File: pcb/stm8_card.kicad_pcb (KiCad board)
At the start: 2 copper layers, 101.9 x 50.9 mm, 22 parts, among them J1 DEBUG HEADER, SW1 TL59AF100Q, SW2 TL59AF100Q, SW3 TL59AF100Q, SW4 TL3302AF260QG, U1 ER-OLED0.91-7, U2 STM8S103F3

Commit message: pcb small edits
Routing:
- net GND: track 150.1 -> 153.8 mm
- net NRST: track 142.9 -> 141.4 mm
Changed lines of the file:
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@@
     (thickness 1.6)
     (drawings 10)
-    (tracks 348)
+    (tracks 347)
     (zones 0)
     (modules 22)
@@
   (page A4)
   (layers
-    (0 F.Cu signal hide)
+    (0 F.Cu signal)
     (31 B.Cu signal)
     (32 B.Adhes user)
@@
     (47 F.CrtYd user)
     (48 B.Fab user)
-    (49 F.Fab user hide)
+    (49 F.Fab user)
   )
   (setup
@@
   (segment (start 232.25 110.25) (end 231.75 110.25) (width 0.25) (layer F.Cu) (net 1))
   (via (at 232.25 110.25) (size 0.8) (drill 0.4) (layers F.Cu B.Cu) (net 1))
-  (via (at 267 106.25) (size 0.8) (drill 0.4) (layers F.Cu B.Cu) (net 1))
+  (via (at 266.75 106) (size 0.8) (drill 0.4) (layers F.Cu B.Cu) (net 1))
   (segment (start 262.975001 103.274999) (end 262.25 104) (width 0.25) (layer B.Cu) (net 1))
   (segment (start 267 106.25) (end 267 104.676998) (width 0.25) (layer B.Cu) (net 1))
-  (segment (start 268.065 117.815) (end 267.25 117) (width 0.25) (layer F.Cu) (net 1))
-  (via (at 267.25 117) (size 0.8) (drill 0.4) (layers F.Cu B.Cu) (net 1))
-  (segment (start 268.9175 117.815) (end 268.065 117.815) (width 0.25) (layer F.Cu) (net 1))
   (segment (start 267 106.25) (end 267 109.75) (width 0.25) (layer B.Cu) (net 1))
   (segment (start 273.975001 132.594999) (end 269.41 137.16) (width 0.25) (layer B.Cu) (net 1))
@@
   (segment (start 260 132.75) (end 253 132.75) (width 0.25) (layer B.Cu) (net 1))
   (segment (start 262 134.75) (end 260 132.75) (width 0.25) (layer B.Cu) (net 1))
+  (via (at 273 114.25) (size 0.8) (drill 0.4) (layers F.Cu B.Cu) (net 1))
+  (segment (start 273 114.47) (end 273 114.25) (width 0.25) (layer F.Cu) (net 1))
+  (segment (start 269.655 117.815) (end 273 114.47) (width 0.25) (layer F.Cu) (net 1))
+  (segment (start 268.9175 117.815) (end 269.655 117.815) (width 0.25) (layer F.Cu) (net 1))
   (segment (start 253.2 105) (end 252.07501 106.12499) (width 0.25) (layer F.Cu) (net 2))
   (segment (start 252.07501 106.12499) (end 245.41251 106.12499) (width 0.25) (layer F.Cu) (net 2))
@@
   (segment (start 222.3 109.2) (end 220.51 109.2) (width 0.25) (layer F.Cu) (net 2))
   (segment (start 248.92 137.16) (end 248.92 129.72) (width 0.25) (layer B.Cu) (net 2))
-  (via (at 235.7 116.5) (size 0.8) (drill 0.4) (layers F.Cu B.Cu) (net 2))
+  (via (at 235.7 115.5) (size 0.8) (drill 0.4) (layers F.Cu B.Cu) (net 2))
   (segment (start 248.92 129.72) (end 235.7 116.5) (width 0.25) (layer B.Cu) (net 2))
   (segment (start 264.6 128.1) (end 266.1 126.6) (width 0.25) (layer F.Cu) (net 2))
@@
   (segment (start 199 147.5) (end 208 147.5) (width 0.25) (layer F.Cu) (net 2))
   (segment (start 235.7 115.5) (end 235.7 113.5) (width 0.25) (layer F.Cu) (net 2))
-  (segment (start 235.7 115.5) (end 235.7 116.75) (width 0.25) (layer F.Cu) (net 2))
+  (segment (start 235.7 116.5) (end 235.7 115.5) (width 0.25) (layer B.Cu) (net 2))
   (segment (start 230.5 104.9625) (end 230.3625 104.9625) (width 0.25) (layer F.Cu) (net 3))
   (segment (start 230.3625 104.9625) (end 228.8 103.4) (width 0.25) (layer F.Cu) (net 3))
@@
   (segment (start 277 114.5) (end 277 107) (width 0.25) (layer F.Cu) (net 13))
   (segment (start 268.228942 115.865) (end 268.9175 115.865) (width 0.25) (layer F.Cu) (net 14))
-  (segment (start 268.9175 115.865) (end 272.235 115.865) (width 0.25) (layer F.Cu) (net 14))
-  (segment (start 272.235 115.865) (end 273 115.1) (width 0.25) (layer F.Cu) (net 14))
-  (segment (start 273 109) (end 275 107) (width 0.25) (layer F.Cu) (net 14))
-  (segment (start 273 115.1) (end 273 109) (width 0.25) (layer F.Cu) (net 14))
-  (via (at 259.7 127.7) (size 0.8) (drill 0.4) (layers F.Cu B.Cu) (net 14))
-  (segment (start 259.75 127.75) (end 259.7 127.7) (width 0.25) (layer F.Cu) (net 14))
+  (via (at 260.75 127.5) (size 0.8) (drill 0.4) (layers F.Cu B.Cu) (net 14))
   (segment (start 242 148.6) (end 262.85 127.75) (width 0.25) (layer F.Cu) (net 14))
-  (segment (start 247.774999 115.774999) (end 259.7 127.7) (width 0.25) (layer B.Cu) (net 14))
-  (segment (start 225.274999 115.774999) (end 247.774999 115.774999) (width 0.25) (layer B.Cu) (net 14))
   (via (at 217.927026 108.725) (size 0.8) (drill 0.4) (layers F.Cu B.Cu) (net 14))
   (segment (start 214.477025 105.274999) (end 217.927026 108.725) (width 0.25) (layer B.Cu) (net 14))
@@
   (segment (start 205.774999 105.651999) (end 206.151999 105.274999) (width 0.25) (layer B.Cu) (net 14))
   (segment (start 205.774999 106.348001) (end 205.774999 105.651999) (width 0.25) (layer B.Cu) (net 14))
-  (segment (start 215.201997 115.774999) (end 205.774999 106.348001) (width 0.25) (layer B.Cu) (net 14))
-  (segment (start 225.274999 115.774999) (end 215.201997 115.774999) (width 0.25) (layer B.Cu) (net 14))
   (segment (start 218.082026 108.57) (end 220.5 108.57) (width 0.25) (layer F.Cu) (net 14))
   (segment (start 217.927026 108.725) (end 218.082026 108.57) (width 0.25) (layer F.Cu) (net 14))
-  (segment (start 265.5 125.1) (end 262.85 127.75) (width 0.25) (layer F.Cu) (net 14))
   (segment (start 265.5 116.25) (end 265.5 125.1) (width 0.25) (layer F.Cu) (net 14))
   (segment (start 265.885 115.865) (end 265.5 116.25) (width 0.25) (layer F.Cu) (net 14))
   (segment (start 268.9175 115.865) (end 265.885 115.865) (width 0.25) (layer F.Cu) (net 14))
-  (segment (start 262.85 127.75) (end 262.75 127.75) (width 0.25) (layer F.Cu) (net 14))
-  (segment (start 262.8 127.7) (end 262.85 127.75) (width 0.25) (layer F.Cu) (net 14))
-  (segment (start 259.7 127.7) (end 262.8 127.7) (width 0.25) (layer F.Cu) (net 14))
+  (segment (start 205.774999 106.348001) (end 214.176998 114.75) (width 0.25) (layer B.Cu) (net 14))
+  (segment (start 248 114.75) (end 260.75 127.5) (width 0.25) (layer B.Cu) (net 14))
+  (segment (start 214.176998 114.75) (end 248 114.75) (width 0.25) (layer B.Cu) (net 14))
+  (segment (start 263.1 127.5) (end 263.175 127.425) (width 0.25) (layer F.Cu) (net 14))
+  (segment (start 260.75 127.5) (end 263.1 127.5) (width 0.25) (layer F.Cu) (net 14))
+  (segment (start 263.175 127.425) (end 262.85 127.75) (width 0.25) (layer F.Cu) (net 14))
+  (segment (start 265.5 125.1) (end 263.175 127.425) (width 0.25) (layer F.Cu) (net 14))
+  (segment (start 275 110.471058) (end 275 107) (width 0.25) (layer F.Cu) (net 14))
+  (segment (start 269.606058 115.865) (end 275 110.471058) (width 0.25) (layer F.Cu) (net 14))
+  (segment (start 268.9175 115.865) (end 269.606058 115.865) (width 0.25) (layer F.Cu) (net 14))
   (segment (start 221.775002 106.71) (end 220.5 106.71) (width 0.25) (layer F.Cu) (net 17))
   (segment (start 223.015012 107.95001) (end 221.775002 106.71) (width 0.25) (layer F.Cu) (net 17))
@@
   (segment (start 265.6 111.8) (end 265.3 111.8) (width 0.25) (layer B.Cu) (net 18))
   (via (at 239 113.7) (size 0.8) (drill 0.4) (layers F.Cu B.Cu) (net 19))
-  (segment (start 239 113.7) (end 239 111.3) (width 0.25) (layer F.Cu) (net 19))
   (segment (start 237.7 111.3) (end 237.5 111.5) (width 0.25) (layer F.Cu) (net 19))
-  (segment (start 239 111.3) (end 237.7 111.3) (width 0.25) (layer F.Cu) (net 19))
   (segment (start 239 113.7) (end 224.273002 113.7) (width 0.25) (layer B.Cu) (net 19))
   (segment (start 220.43 107.4) (end 220.5 107.33) (width 0.25) (layer F.Cu) (net 19))
@@
   (segment (start 265.55 113.7) (end 239 113.7) (width 0.25) (layer B.Cu) (net 19))
   (segment (start 265.8 113.7) (end 265.55 113.7) (width 0.25) (layer B.Cu) (net 19))
+  (segment (start 238.25 111.5) (end 239 112.25) (width 0.25) (layer F.Cu) (net 19))
+  (segment (start 237.5 111.5) (end 238.25 111.5) (width 0.25) (layer F.Cu) (net 19))
+  (segment (start 239 113.7) (end 239 112.25) (width 0.25) (layer F.Cu) (net 19))
   (segment (start 273.91859 116.515) (end 274.6425 116.515) (width 0.25) (layer F.Cu) (net 20))
   (via (at 268.8 131.2) (size 0.8) (drill 0.4) (layers F.Cu B.Cu) (net 20))

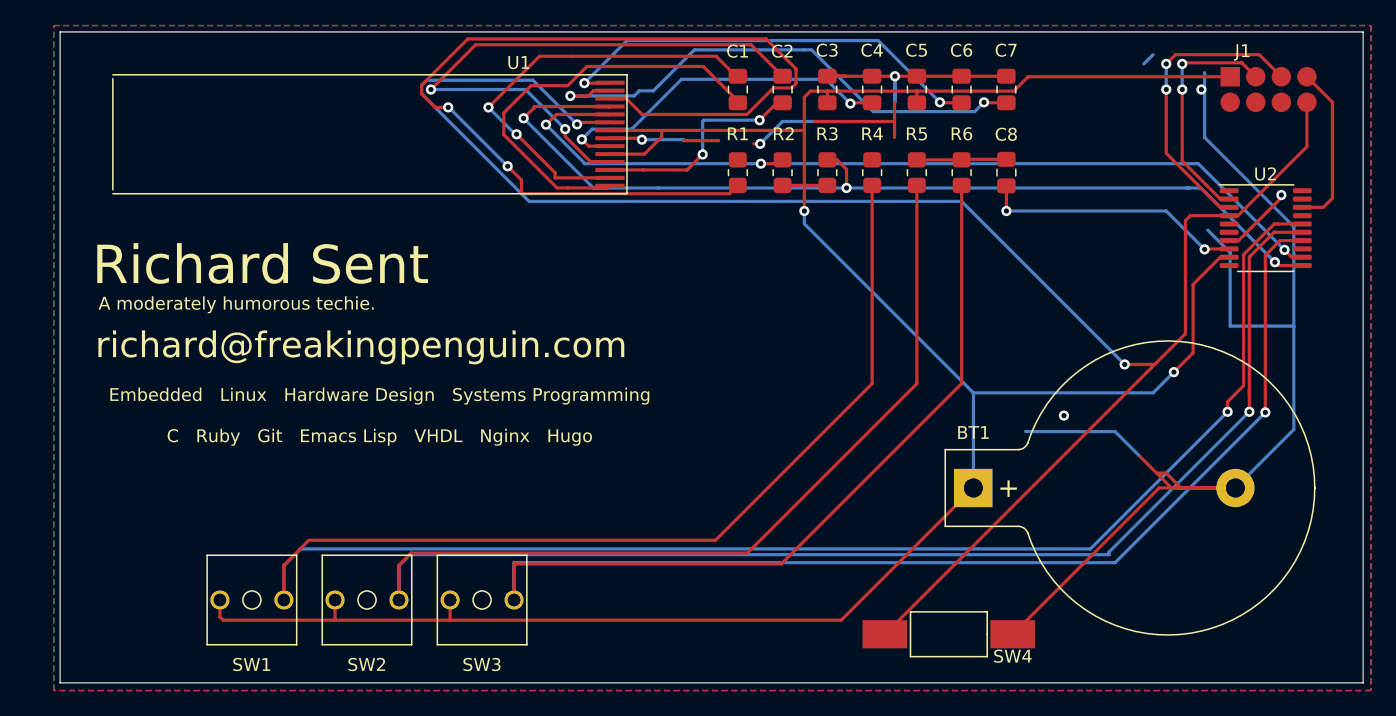
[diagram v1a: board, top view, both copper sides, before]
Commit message: pcb hid ground via under mcu
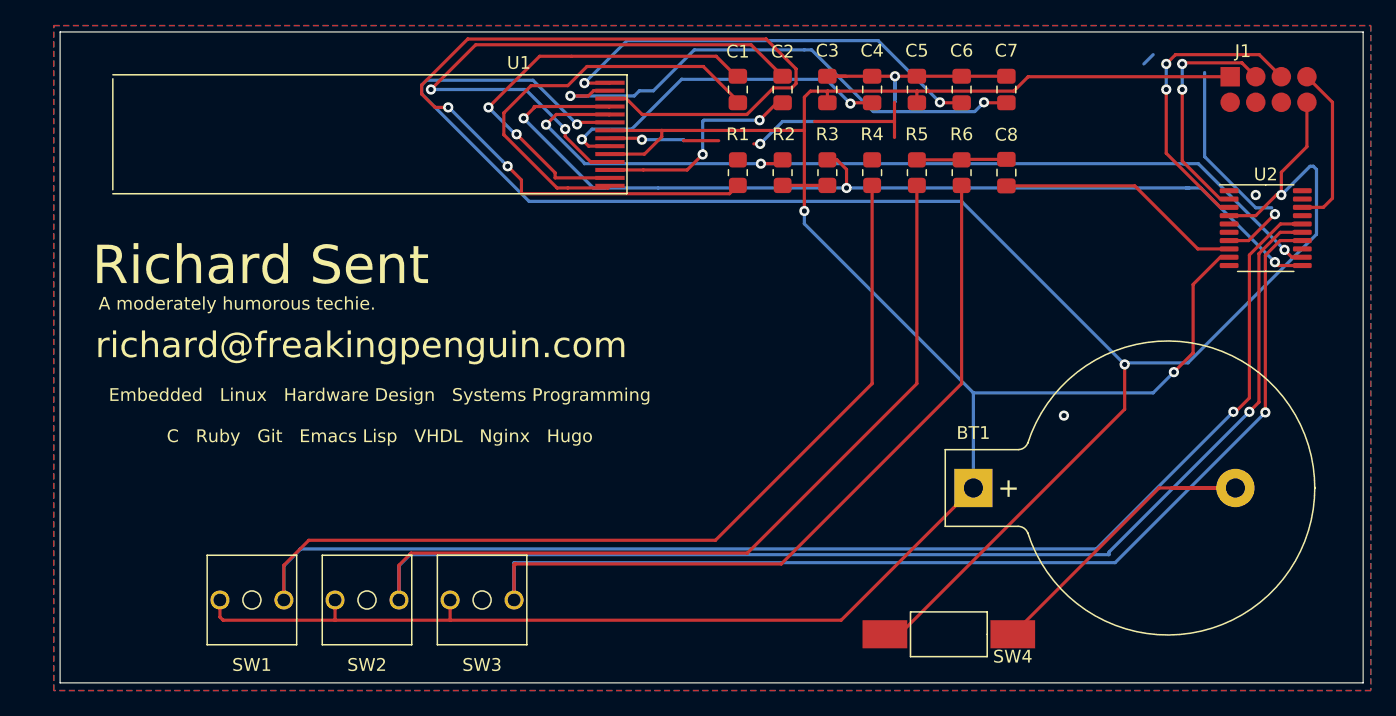
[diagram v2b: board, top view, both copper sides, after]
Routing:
- net GND: track 153.8 -> 100.0 mm
- net NRST: track 141.4 -> 151.3 mm, vias 2 -> 3
- net Net-(C8-Pad1): track 20.6 -> 19.5 mm, vias 2 -> 0
- net btn1: track 157.1 -> 156.4 mm

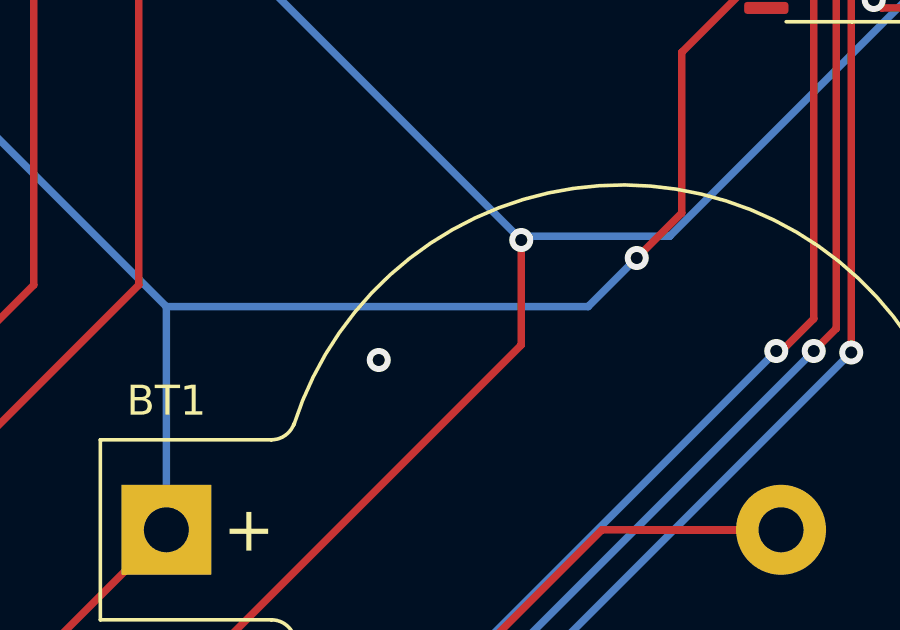
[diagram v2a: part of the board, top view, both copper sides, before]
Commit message: pcb moved some vias a tiny bit
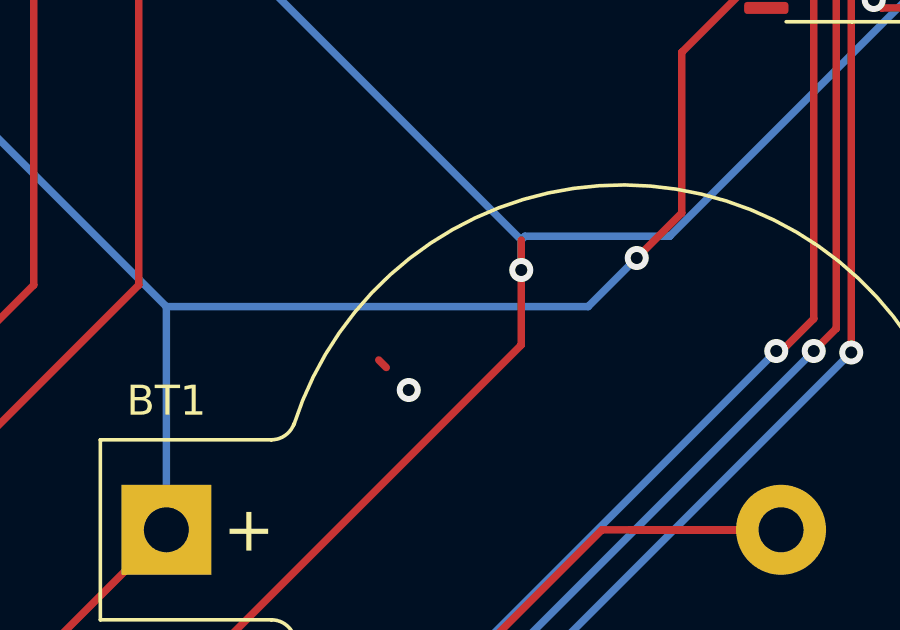
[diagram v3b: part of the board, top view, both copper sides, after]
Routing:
- net NRST: track 151.3 -> 152.3 mm
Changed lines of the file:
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@@
     (thickness 1.6)
     (drawings 10)
-    (tracks 331)
+    (tracks 333)
     (zones 0)
     (modules 22)
@@
   (segment (start 269.41 137.16) (end 265.16 137.16) (width 0.25) (layer F.Cu) (net 1))
   (segment (start 269.41 137.16) (end 264.41 137.16) (width 0.25) (layer F.Cu) (net 1))
-  (via (at 256 131.5) (size 0.8) (drill 0.4) (layers F.Cu B.Cu) (net 1))
+  (via (at 257 132.5) (size 0.8) (drill 0.4) (layers F.Cu B.Cu) (net 1))
   (via (at 272.5 115.75) (size 0.8) (drill 0.4) (layers F.Cu B.Cu) (net 1))
   (segment (start 267 111.25) (end 267 106.25) (width 0.25) (layer B.Cu) (net 1))
@@
   (segment (start 270.435 117.815) (end 272.5 115.75) (width 0.25) (layer F.Cu) (net 1))
   (segment (start 268.9175 117.815) (end 270.435 117.815) (width 0.25) (layer F.Cu) (net 1))
+  (segment (start 256 131.5) (end 256.25 131.75) (width 0.25) (layer F.Cu) (net 1))
   (segment (start 253.2 105) (end 252.07501 106.12499) (width 0.25) (layer F.Cu) (net 2))
   (segment (start 252.07501 106.12499) (end 245.41251 106.12499) (width 0.25) (layer F.Cu) (net 2))
@@
   (segment (start 205.774999 106.348001) (end 205.774999 105.651999) (width 0.25) (layer B.Cu) (net 14))
   (segment (start 217.927026 108.725) (end 218.082026 108.57) (width 0.25) (layer F.Cu) (net 14))
-  (via (at 260.75 127.5) (size 0.8) (drill 0.4) (layers F.Cu B.Cu) (net 14))
+  (via (at 260.75 128.5) (size 0.8) (drill 0.4) (layers F.Cu B.Cu) (net 14))
   (segment (start 214.176998 114.75) (end 248 114.75) (width 0.25) (layer B.Cu) (net 14))
   (segment (start 205.774999 106.348001) (end 214.176998 114.75) (width 0.25) (layer B.Cu) (net 14))
@@
   (segment (start 265.698003 127.374999) (end 275.75 117.323002) (width 0.25) (layer B.Cu) (net 14))
   (segment (start 260.875001 127.374999) (end 265.698003 127.374999) (width 0.25) (layer B.Cu) (net 14))
-  (segment (start 260.75 127.5) (end 260.875001 127.374999) (width 0.25) (layer B.Cu) (net 14))
   (segment (start 242 148.6) (end 243.15 148.6) (width 0.25) (layer F.Cu) (net 14))
   (segment (start 260.75 131) (end 260.75 127.5) (width 0.25) (layer F.Cu) (net 14))
@@
   (segment (start 273 112.471058) (end 275 110.471058) (width 0.25) (layer F.Cu) (net 14))
   (segment (start 273 114.25) (end 273 112.471058) (width 0.25) (layer F.Cu) (net 14))
+  (segment (start 260.875001 127.374999) (end 260.75 127.5) (width 0.25) (layer B.Cu) (net 14))
+  (segment (start 260.75 127.5) (end 260.75 128.5) (width 0.25) (layer B.Cu) (net 14))
   (segment (start 221.775002 106.71) (end 220.5 106.71) (width 0.25) (layer F.Cu) (net 17))
   (segment (start 223.015012 107.95001) (end 221.775002 106.71) (width 0.25) (layer F.Cu) (net 17))
